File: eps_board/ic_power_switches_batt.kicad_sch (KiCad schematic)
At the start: 6 parts, among them U53 MCP23008T-E/SS

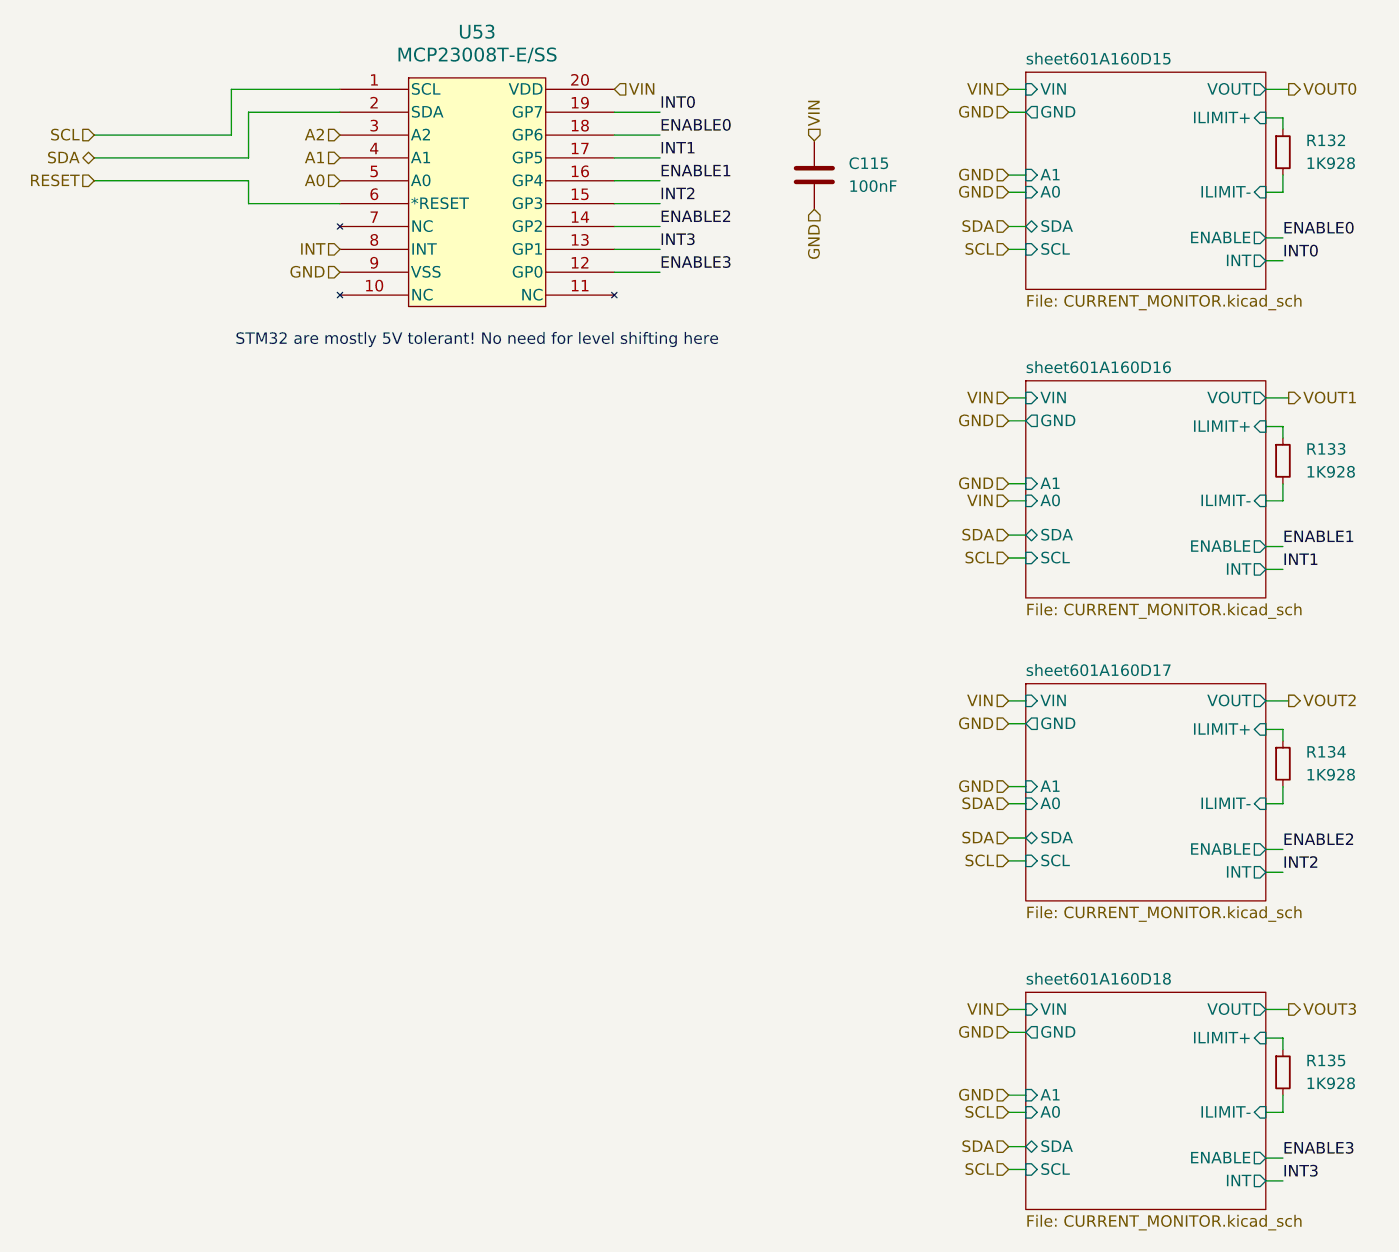
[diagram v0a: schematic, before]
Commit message: cleaning up bom: remove main camera port since it has not pullups and capacitors, correcting some errors in camera switch
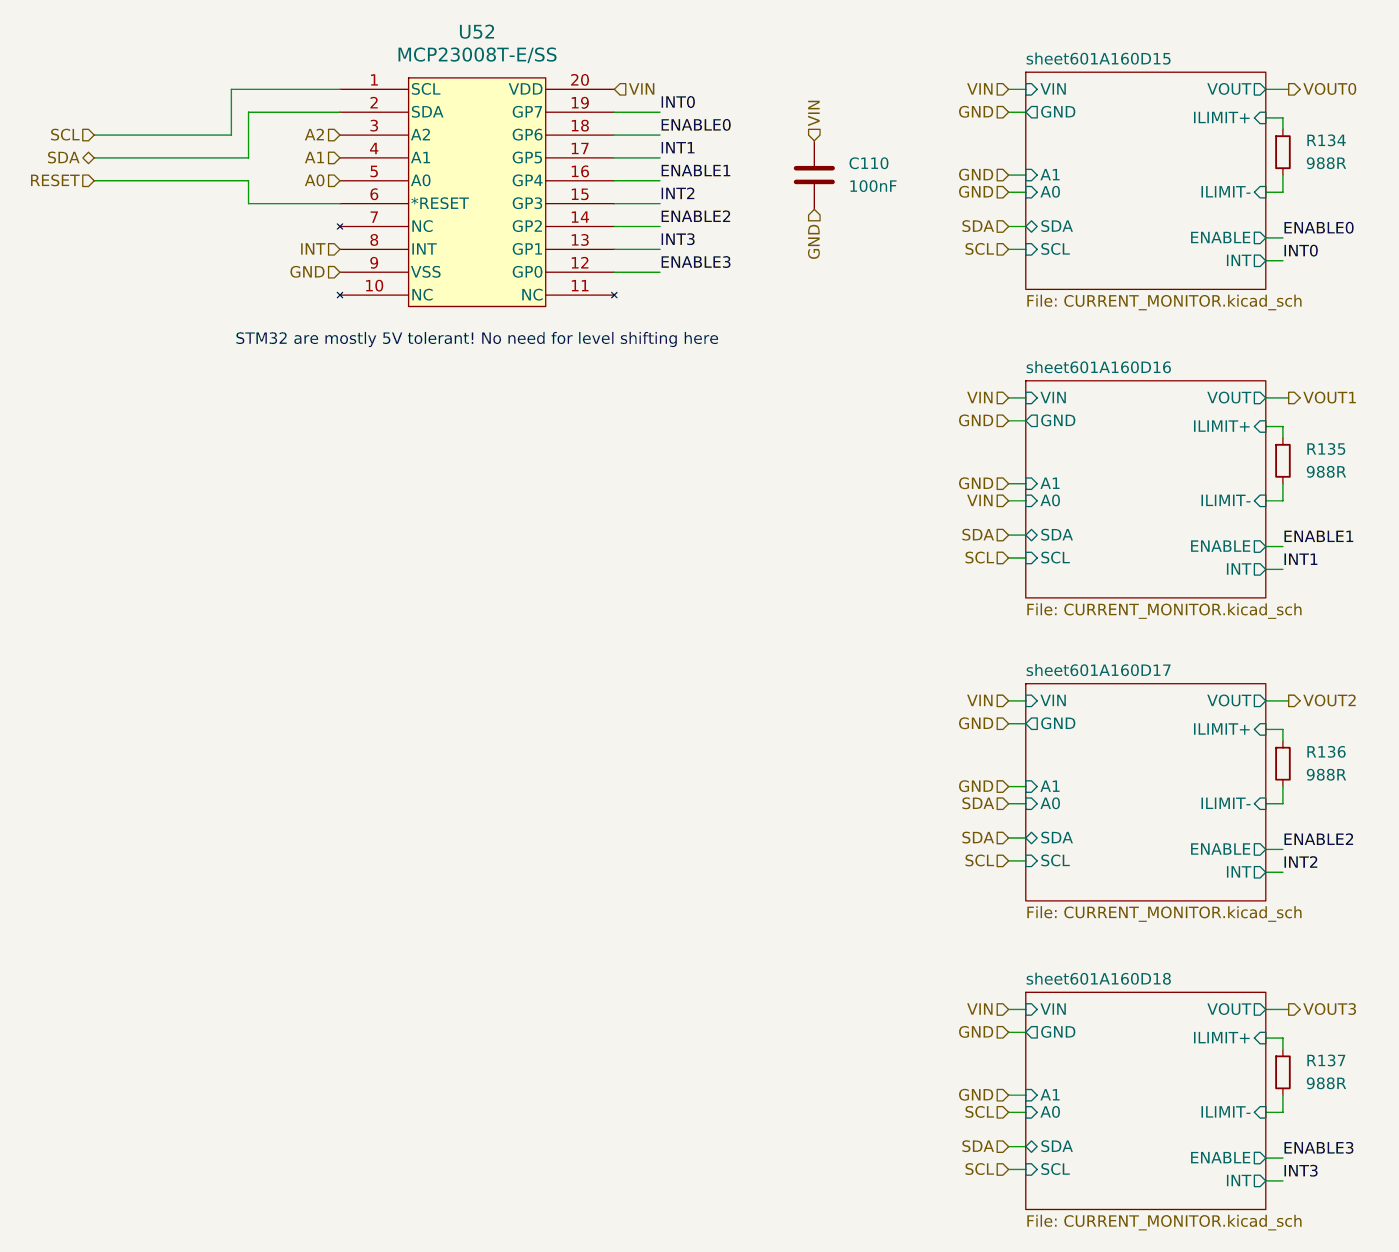
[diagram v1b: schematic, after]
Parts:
- R134: renamed from R132; value 1K928 -> 988R; Part Number RC0603FR-071K928L -> RT0603DRE07988RL; Tolerance 1 -> 0.5
- R135: renamed from R133; value 1K928 -> 988R; Part Number RC0603FR-071K928L -> RT0603DRE07988RL; Tolerance 1 -> 0.5
- R136: renamed from R134; value 1K928 -> 988R; Part Number RC0603FR-071K928L -> RT0603DRE07988RL; Tolerance 1 -> 0.5
- R137: renamed from R135; value 1K928 -> 988R; Part Number RC0603FR-071K928L -> RT0603DRE07988RL; Tolerance 1 -> 0.5
- renumbered C115 to C110, U53 to U52
